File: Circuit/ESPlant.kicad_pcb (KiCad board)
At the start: 2 copper layers, 97 x 77.5 mm, 75 parts, among them P1 SOIL, P101 CONN_DIGITAL, P102 CONN_ANALOG, P103 CONN_SERIAL, P104 CONN_I2C, P105 SOLAR, P106 USB_5PIN_SHELL, P109 CONN_PWR, P110 CONN_01X05, P111 UV, P112 TEMP, P113 NEOPIXEL, P114 PIR, Q101 FDN340P, Q201 FDN340P, Q202 FDN340P, Q203 FDN340P, SW101 RESET, SW102 PRGM, SW103 RESET, SW104 SS12D00, U101 STM32F042F, U103 ESP-12E, U201 CN3063, U202 MCP6002, U301 BME280, U302 ADXL345

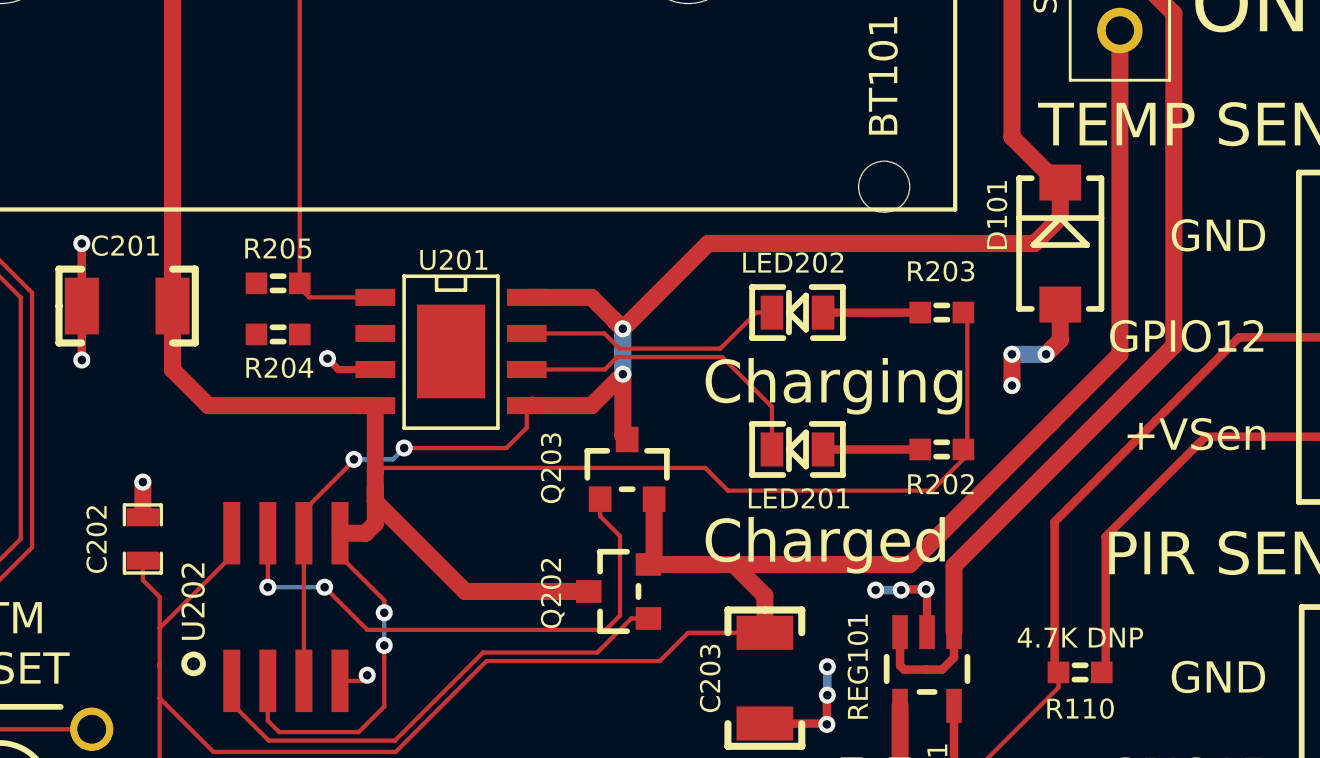
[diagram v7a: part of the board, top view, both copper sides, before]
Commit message: Combine series resistors on CN3063 CHRG/DONE, thanks @GeoffLethbridge for the tip
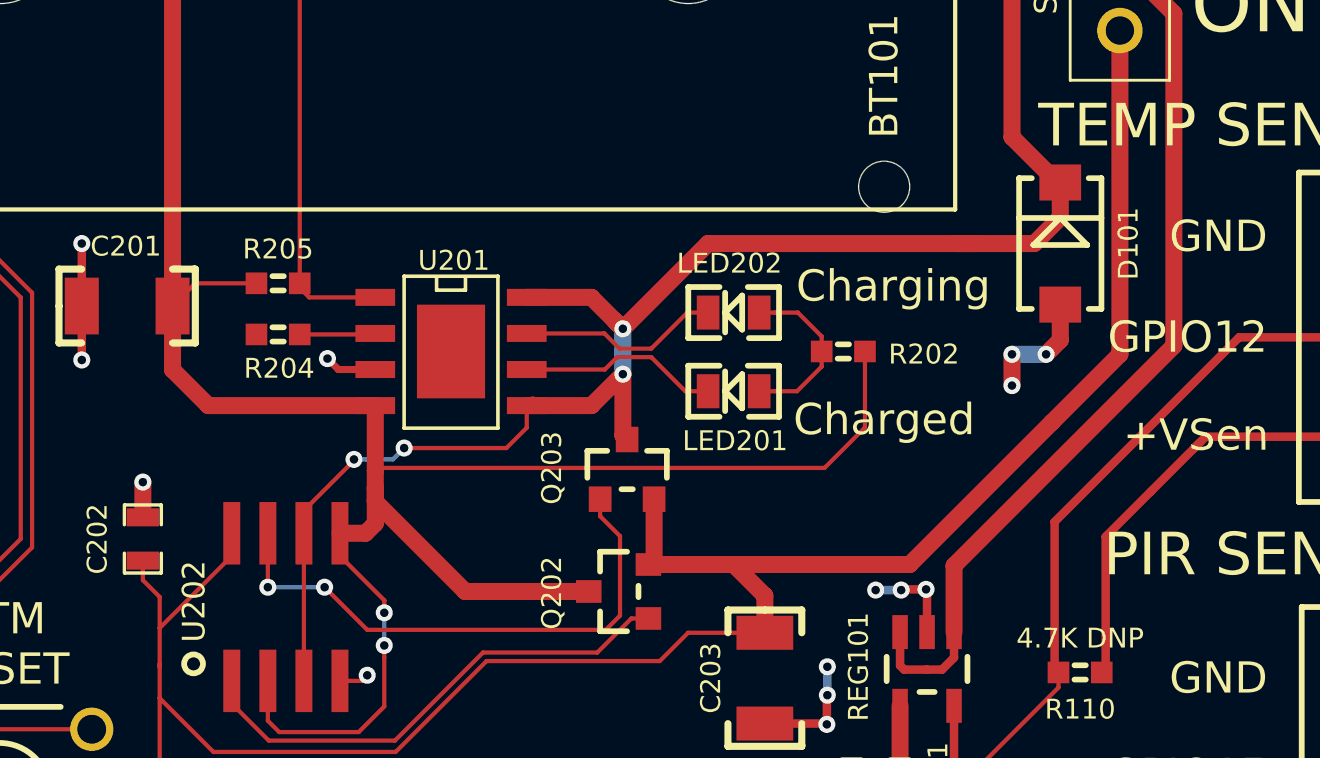
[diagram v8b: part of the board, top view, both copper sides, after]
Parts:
- removed R203: 1K, FT:0603
- moved R202 4.89 mm to (216.1, 84.1)
- moved LED201 3.04 mm to (212.2, 85.5)
- moved LED202 2.25 mm to (212.2, 82.7)
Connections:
- LED202 pad A: Net-(LED202-PadA) -> Net-(LED201-PadA)
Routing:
- net /Power/~DONE: track 11.0 -> 7.06 mm
- net Net-(LED202-PadA): track 3.28 -> 0.00 mm
- net /Power/VIN: track 116.6 -> 113.7 mm
- net Net-(LED201-PadA): track 3.28 -> 6.17 mm
- net Net-(R204-Pad1): track 0.00 -> 2.67 mm
- net /Power/~CHRG: track 9.38 -> 7.13 mm
